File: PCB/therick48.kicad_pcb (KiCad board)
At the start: 2 copper layers, 226.5 x 75.8 mm, 133 parts, among them J1 TYPE-C-31-M12_13, J2 AVR-ISP-6_mod, K1 KEYSW, K10 KEYSW, K11 KEYSW, K12 KEYSW, K13 KEYSW, K14 KEYSW, K15 KEYSW, K16 KEYSW, K17 KEYSW, K18 KEYSW, K19 KEYSW, K2 KEYSW, K20 KEYSW, K21 KEYSW, K22 KEYSW, K23 KEYSW, K24 KEYSW, K25 KEYSW, K26 KEYSW, K27 KEYSW, K28 KEYSW, K29 KEYSW, K3 KEYSW, K30 KEYSW, K31 KEYSW, K32 KEYSW, K33 KEYSW, K34 KEYSW, K35 KEYSW, K36 KEYSW, K37 KEYSW, K38 KEYSW, K39 KEYSW, K4 KEYSW, K40 KEYSW, K41 KEYSW, K42 KEYSW, K43 KEYSW, K44 KEYSW, K45 KEYSW, K46 KEYSW, K47 KEYSW, K48 KEYSW, K5 KEYSW, K6 KEYSW, K7 KEYSW, K8 KEYSW, K9 KEYSW, SW1 SW_PUSH, U1 ATMEGA32U4, U2 HOLE, U3 USBLC6-2SC6, U4 HOLE, Y1 16MHz

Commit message: .
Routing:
- net VCC: vias 7 -> 6
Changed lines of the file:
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@@
     (thickness 1.6)
     (drawings 23)
-    (tracks 643)
+    (tracks 642)
     (zones 0)
     (modules 133)
@@
     (35 F.Paste user)
     (36 B.SilkS user)
-    (37 F.SilkS user)
+    (37 F.SilkS user hide)
     (38 B.Mask user)
     (39 F.Mask user)
@@
   (segment (start 257.289 106.54) (end 261.94 106.54) (width 0.25) (layer B.Cu) (net 48))
   (segment (start 256.54 101.551375) (end 256.54 105.791) (width 0.25) (layer B.Cu) (net 48))
-  (via (at 96.7105 51.3715) (size 0.5) (drill 0.25) (layers F.Cu B.Cu) (net 49))
   (segment (start 81.153 62.945) (end 81.153 55.245) (width 0.4) (layer B.Cu) (net 49))
   (segment (start 82.427 64.219) (end 81.153 62.945) (width 0.4) (layer B.Cu) (net 49))
@@
   (segment (start 95.803635 60.279365) (end 91.58322 60.279365) (width 0.25) (layer F.Cu) (net 49))
   (segment (start 96.7105 59.3725) (end 95.803635 60.279365) (width 0.25) (layer F.Cu) (net 49))
-  (segment (start 96.7105 51.3715) (end 96.7105 59.3725) (width 0.25) (layer F.Cu) (net 49))
   (segment (start 87.9745 61.595) (end 88.011 61.595) (width 0.25) (layer B.Cu) (net 49))
   (via (at 88.011 61.595) (size 0.5) (drill 0.25) (layers F.Cu B.Cu) (net 49))
@@
   (segment (start 161.656 50.15) (end 159.7768 50.15) (width 0.25) (layer B.Cu) (net 49))
   (segment (start 162.052 50.546) (end 161.656 50.15) (width 0.25) (layer B.Cu) (net 49))
+  (segment (start 96.7105 51.3715) (end 96.7105 59.3725) (width 0.25) (layer B.Cu) (net 49))
   (segment (start 85.725 52.959) (end 89.535 52.959) (width 0.25) (layer B.Cu) (net 50))
   (segment (start 85.09 50.968) (end 85.09 52.324) (width 0.25) (layer B.Cu) (net 50))

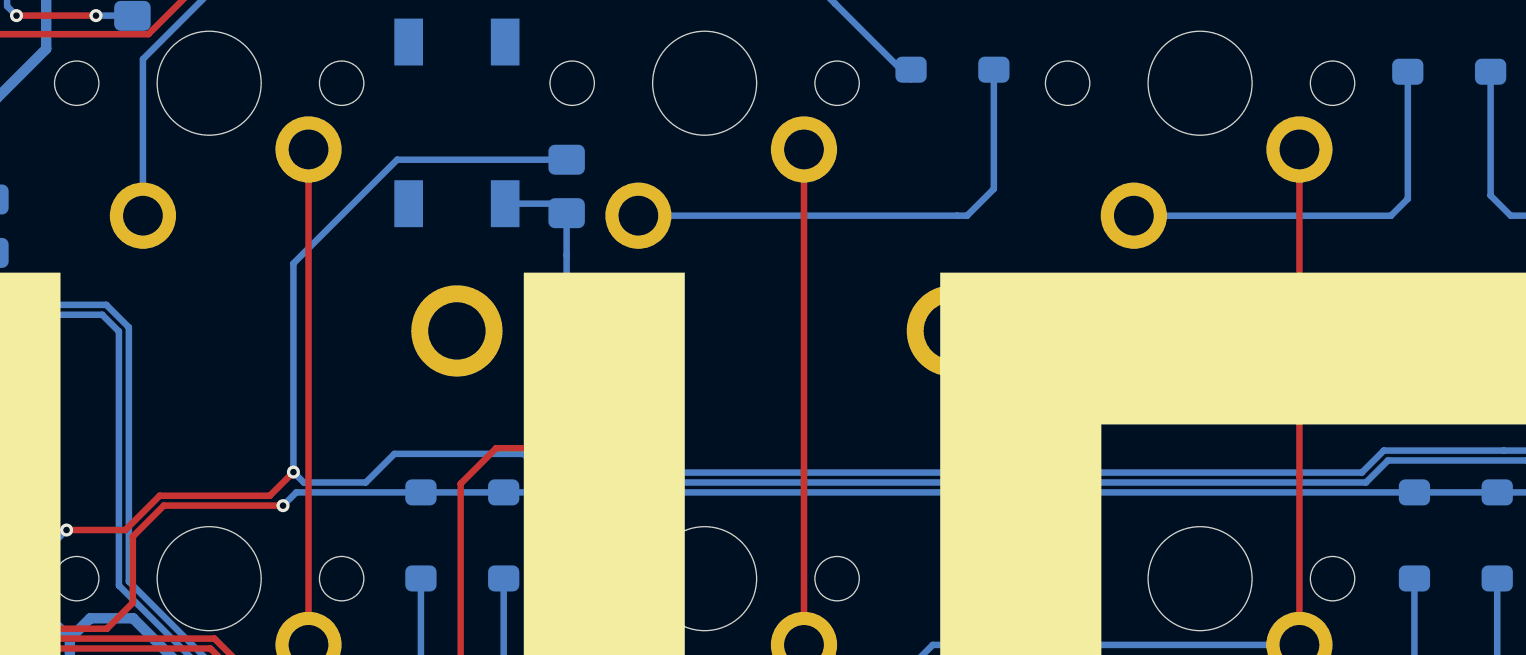
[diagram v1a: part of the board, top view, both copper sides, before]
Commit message: Changed a trace
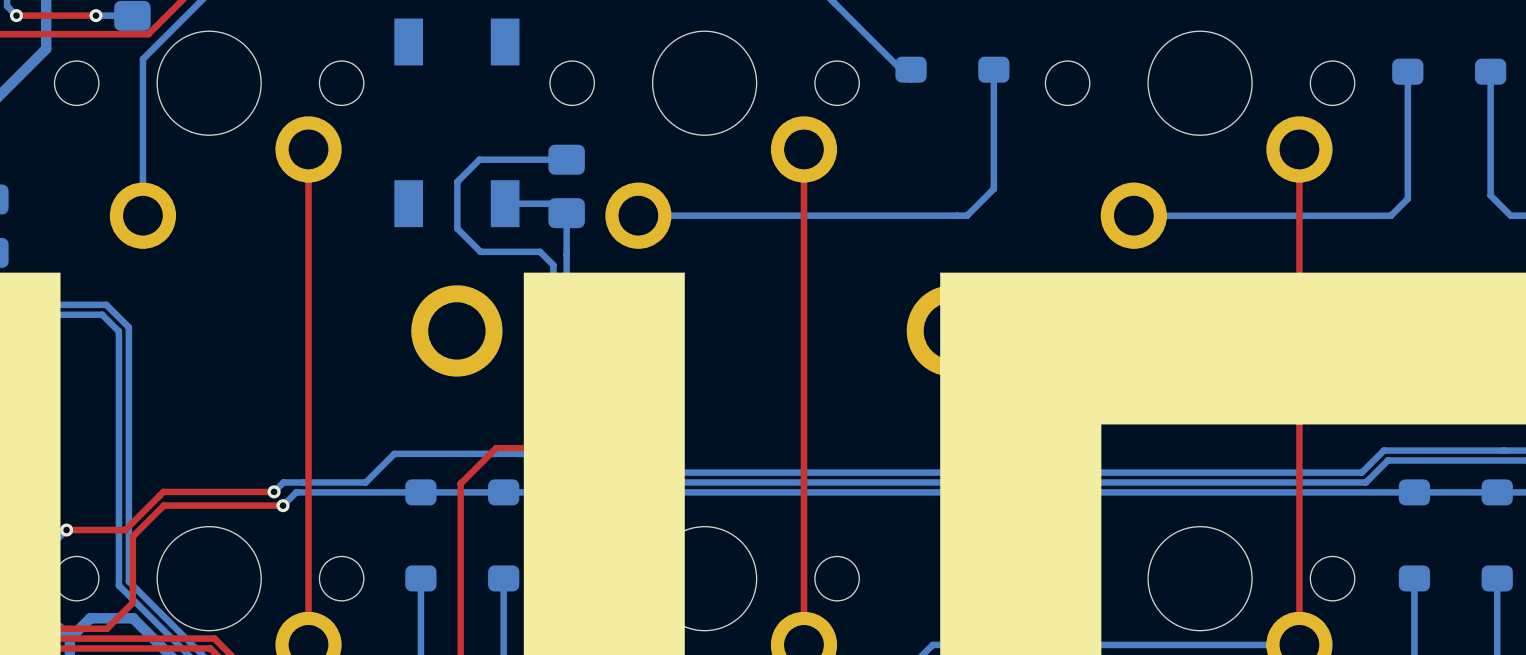
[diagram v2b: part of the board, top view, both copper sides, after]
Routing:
- net VCC: track 231.4 -> 228.8 mm
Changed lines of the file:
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@@
     (thickness 1.6)
     (drawings 23)
-    (tracks 642)
+    (tracks 648)
     (zones 0)
     (modules 133)
@@
   (segment (start 89.027 91.392) (end 89.019 91.4) (width 0.4) (layer B.Cu) (net 49))
   (segment (start 89.027 85.217) (end 89.027 91.392) (width 0.4) (layer B.Cu) (net 49))
-  (segment (start 96.7105 51.3715) (end 100.68825 47.39375) (width 0.25) (layer B.Cu) (net 49))
   (segment (start 82.427 64.219) (end 85.3505 64.219) (width 0.4) (layer B.Cu) (net 49))
   (segment (start 92.864761 70.697739) (end 92.2375 71.325) (width 0.4) (layer B.Cu) (net 49))
@@
   (segment (start 76.199 70.741) (end 80.011 66.929) (width 0.4) (layer F.Cu) (net 49))
   (segment (start 91.58322 60.279365) (end 90.267585 61.595) (width 0.25) (layer F.Cu) (net 49))
-  (segment (start 95.803635 60.279365) (end 91.58322 60.279365) (width 0.25) (layer F.Cu) (net 49))
-  (segment (start 96.7105 59.3725) (end 95.803635 60.279365) (width 0.25) (layer F.Cu) (net 49))
   (segment (start 87.9745 61.595) (end 88.011 61.595) (width 0.25) (layer B.Cu) (net 49))
   (via (at 88.011 61.595) (size 0.5) (drill 0.25) (layers F.Cu B.Cu) (net 49))
@@
   (segment (start 88.265 84.455) (end 90.551 84.455) (width 0.4) (layer F.Cu) (net 49))
   (segment (start 94.361 77.597) (end 90.551 81.407) (width 0.4) (layer F.Cu) (net 49))
-  (via (at 96.7105 59.3725) (size 0.5) (drill 0.25) (layers F.Cu B.Cu) (net 49))
-  (segment (start 100.68825 47.39375) (end 107.188 47.39375) (width 0.25) (layer B.Cu) (net 49))
   (segment (start 99.486635 59.771365) (end 97.109365 59.771365) (width 0.25) (layer B.Cu) (net 49))
   (segment (start 105.537 58.674) (end 100.584 58.674) (width 0.25) (layer B.Cu) (net 49))
-  (segment (start 106.634365 59.771365) (end 105.537 58.674) (width 0.25) (layer B.Cu) (net 49))
-  (segment (start 97.109365 59.771365) (end 96.7105 59.3725) (width 0.25) (layer B.Cu) (net 49))
-  (segment (start 137.840635 59.771365) (end 106.634365 59.771365) (width 0.25) (layer B.Cu) (net 49))
   (segment (start 100.584 58.674) (end 99.486635 59.771365) (width 0.25) (layer B.Cu) (net 49))
   (segment (start 138.684 58.928) (end 137.840635 59.771365) (width 0.25) (layer B.Cu) (net 49))
@@
   (segment (start 161.656 50.15) (end 159.7768 50.15) (width 0.25) (layer B.Cu) (net 49))
   (segment (start 162.052 50.546) (end 161.656 50.15) (width 0.25) (layer B.Cu) (net 49))
-  (segment (start 96.7105 51.3715) (end 96.7105 59.3725) (width 0.25) (layer B.Cu) (net 49))
+  (segment (start 137.840635 59.771365) (end 107.777365 59.771365) (width 0.25) (layer B.Cu) (net 49))
+  (via (at 95.968694 60.131537) (size 0.5) (drill 0.25) (layers F.Cu B.Cu) (net 49))
+  (segment (start 96.328866 59.771365) (end 95.968694 60.131537) (width 0.25) (layer B.Cu) (net 49))
+  (segment (start 97.109365 59.771365) (end 96.328866 59.771365) (width 0.25) (layer B.Cu) (net 49))
+  (segment (start 91.731048 60.131537) (end 91.58322 60.279365) (width 0.25) (layer F.Cu) (net 49))
+  (segment (start 95.968694 60.131537) (end 91.731048 60.131537) (width 0.25) (layer F.Cu) (net 49))
+  (segment (start 106.68 58.674) (end 107.777365 59.771365) (width 0.25) (layer B.Cu) (net 49))
+  (segment (start 106.172 50.927) (end 106.68 51.435) (width 0.25) (layer B.Cu) (net 49))
+  (segment (start 102.997 50.038) (end 103.886 50.927) (width 0.25) (layer B.Cu) (net 49))
+  (segment (start 102.997 48.242602) (end 102.997 50.038) (width 0.25) (layer B.Cu) (net 49))
+  (segment (start 106.68 51.435) (end 106.68 58.674) (width 0.25) (layer B.Cu) (net 49))
+  (segment (start 103.886 50.927) (end 106.172 50.927) (width 0.25) (layer B.Cu) (net 49))
+  (segment (start 103.845852 47.39375) (end 102.997 48.242602) (width 0.25) (layer B.Cu) (net 49))
+  (segment (start 107.188 47.39375) (end 103.845852 47.39375) (width 0.25) (layer B.Cu) (net 49))
+  (segment (start 105.537 58.674) (end 106.68 58.674) (width 0.25) (layer B.Cu) (net 49))
   (segment (start 85.725 52.959) (end 89.535 52.959) (width 0.25) (layer B.Cu) (net 50))
   (segment (start 85.09 50.968) (end 85.09 52.324) (width 0.25) (layer B.Cu) (net 50))
